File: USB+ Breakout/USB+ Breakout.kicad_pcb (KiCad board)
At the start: 2 copper layers, 15.2 x 50.8 mm, 8 parts, among them J101 Conn_01x10, J201 USB_C_Receptacle, J202 USB_C_Receptacle, J301 Conn_01x10

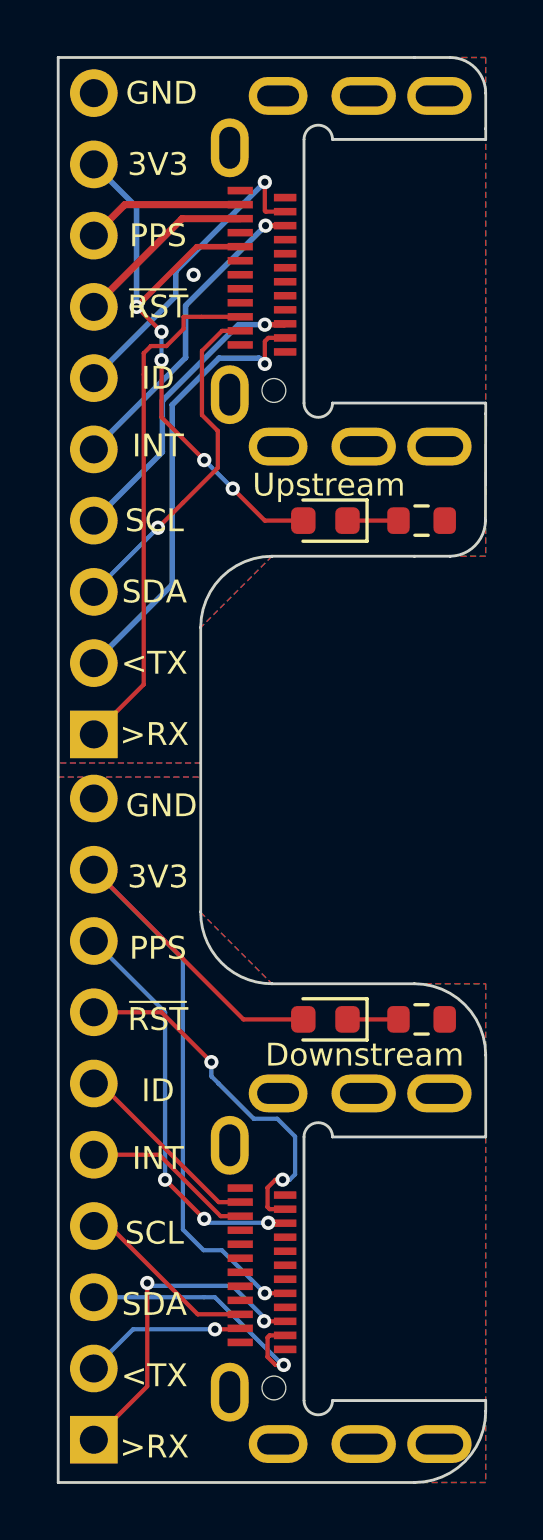
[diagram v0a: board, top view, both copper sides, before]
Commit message: Updated LEDs and edge cutouts
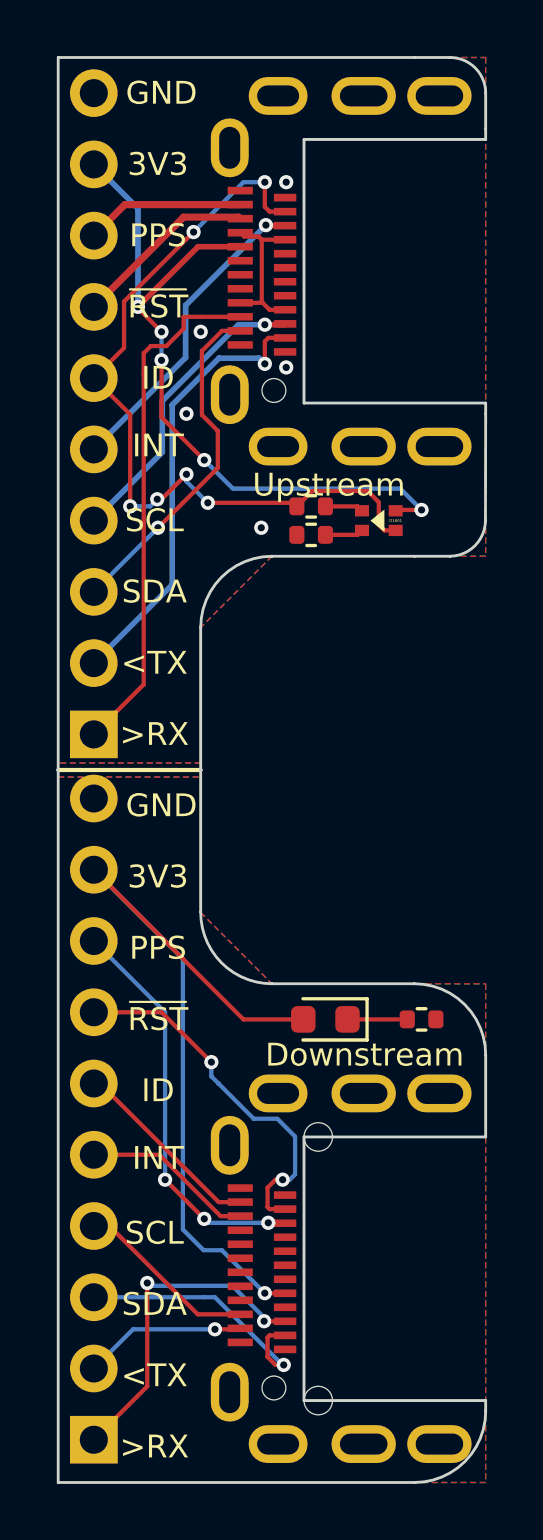
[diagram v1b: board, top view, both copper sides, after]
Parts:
- removed D101: RED, LED_SMD:LED_0603_1608Metric
- removed R101: 1.5k, Resistor_SMD:R_0603_1608Metric
- added D1601: GREEN, YELLOW, KwanSystems:LEDKingbrightAPHB, F.Cu at (135.9, 92.7)
- added R1601: 330, Resistor_SMD:R_0402_1005Metric, F.Cu at (133.5, 93.2)
- added R1602: 1.5k, Resistor_SMD:R_0402_1005Metric, F.Cu at (133.5, 92.2)
- R301: footprint Resistor_SMD:R_0603_1608Metric -> Resistor_SMD:R_0402_1005Metric
- renumbered J201 to J1601, J202 to J1602
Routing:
- net /USB Cable/P_ID: track 11.3 -> 28.6 mm, vias 1 -> 6
- net unconnected-(J1601-PadA4): track 0.00 -> 5.67 mm
- net /USB Cable/P_3V3: track 21.2 -> 26.1 mm
- net Net-(D101-Pad1): track 1.82 -> 0.00 mm
- net /USB Cable/DY-: track 0.00 -> 1.37 mm
- net /USB Cable/DG-: track 0.00 -> 1.37 mm
- net /USB Cable/P_GND: vias 1 -> 5
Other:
- outline, holes or cut-outs redrawn
- board text added: "Drill"
- board text added: "Slot"
- board text added: "USB+ Breakout 1.1 22 Apr 2022"
- board text removed: "USB+ Breakout"
